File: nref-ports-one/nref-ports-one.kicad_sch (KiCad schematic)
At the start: 153 parts, among them J1 CONN_HEAD, J10 CONN_SPK, J11 POWSW, J12 SBU, J2 DM3AT-SF-PEJM5, J3 09452812561, J4 USB_C_Receptacle, J5 Conn_01x10_Pin, J6 Conn_01x14_Pin, J7 Conn_01x12_Pin, J8 PWR, J9 Conn_01x10_Pin, SW1 SW_Push, U1 TPS7A0533PDBZ, U10 LMR51430, U11 TPS66021YBGR, U12 TLV75518PDBV, U13 TMUXHS4212, U14 EQCO5X31C0-I_6NX, U15 LP5907MFX-1.2, U2 TLV320AIC3100, U3 TXS0108EPW, U4 SN74AVC1T45, U5 TPD4E02B04DQA, U6 TPD4E02B04DQA, U7 TPD4E02B04DQA, U8 FUSB302BMPX, U9 PCA9557RGVR

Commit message: ports left/one fixes
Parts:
- R45, R46: value 33 -> 0; LCSC C25105 -> C17168; Manufacturer Yageo -> Panasonic; Manufacturer_No RC0402FR-0733RL -> ERJ2GE0R00X
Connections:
- net SBU_R_P: now reaches J12.2 (Pin_2), R46.1
- net SBU_R_N: now reaches J12.1 (Pin_1), R45.1
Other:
- note added: "TODO: currently not connected"
- note removed: "TODO: move all the way up on board"
- note removed: "currently not connected"
- moved on the sheet: J12, R45, R46
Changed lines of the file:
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@@
 (kicad_sch
-	(version 20250114)
+	(version 20260306)
 	(generator "eeschema")
-	(generator_version "9.0")
+	(generator_version "10.0")
 	(paper "A2" portrait)

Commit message: clean up major schematics for book
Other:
- note added: "1GBe to mainboard"
- note added: "Audio DAC/ADC"
- note added: "I2S Audio to mainboard"
- note added: "Luxury Edition"
- note added: "NOTE: currently not connected"
- note added: "Port Board One (Left)"
- note added: "SD Card to mainboard"
- note added: "System Controller Remote GPIO Bank"
- note added: "USB3 to mainboard"
- note removed: "1GBe to motherboard"
- note removed: "Audio"
- note removed: "I2S Audio"
- note removed: "SD Card"
- note removed: "Sysctl GPIO Bank"
- note removed: "TODO: currently not connected"
- note removed: "USB3 to port farm 1"
- note removed: "fixed: swapped SRC and SINK EN"
- note removed: "fixed: wrong pinout/footprint (tssop vs qfn)"
- company: (none) -> MNT Research GmbH, Copyright 2026
- title: (none) -> MNT Reform Next Port Board One
- moved on the sheet: C1, C10, C11, C12, C13, C14, C15, C16, C17, C18, C19, C2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
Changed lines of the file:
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@@
 	(generator_version "10.0")
 	(paper "A2" portrait)
+	(title_block
+		(title "MNT Reform Next Port Board One")
+		(date "2026-06-01")
+		(rev "R-1")
+		(company "MNT Research GmbH, Copyright 2026")
+		(comment 1 "Engineer: Lucie L. Hartmann")
+		(comment 2 "License: CERN OHL-S 2.0")
+		(comment 3 "https://mntre.com")
+	)

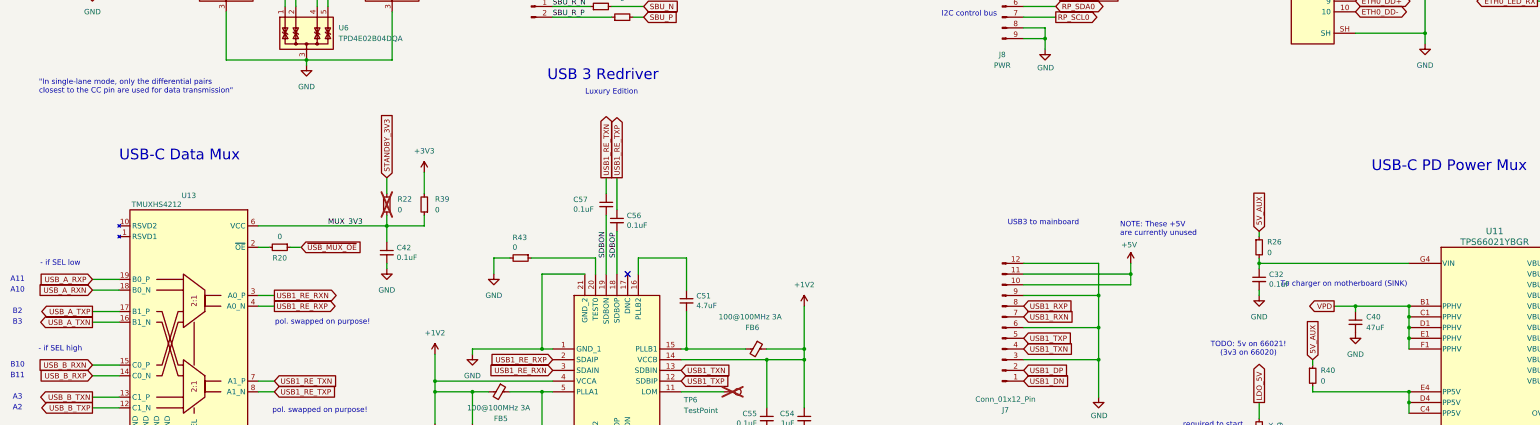
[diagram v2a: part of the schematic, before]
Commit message: small schematic cleanups for book
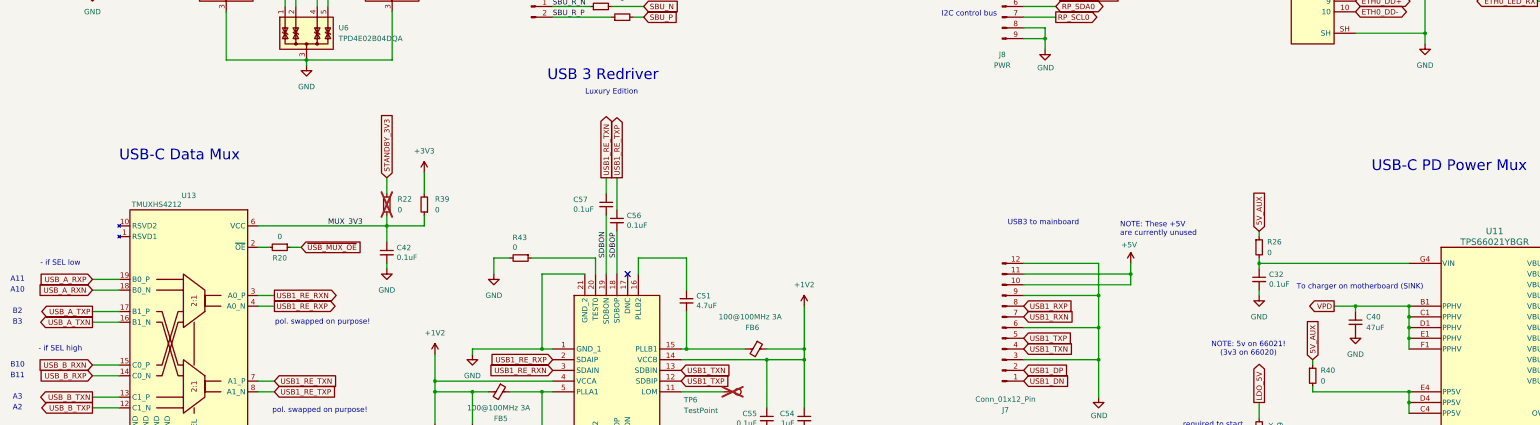
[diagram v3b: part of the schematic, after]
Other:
- note added: "NOTE: 5v on 66021! (3v3 on 66020)"
- note removed: ""In single-lane mode, only the differential pairs closest to the CC pin are used for data transmission""
- note removed: "TODO: 5v on 66021! (3v3 on 66020)"
